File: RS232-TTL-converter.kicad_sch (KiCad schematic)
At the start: 21 parts, among them J1 DE9_Socket, J13 430450600, Q2 BS170F, Q3 BS170F, U4 MAX3232

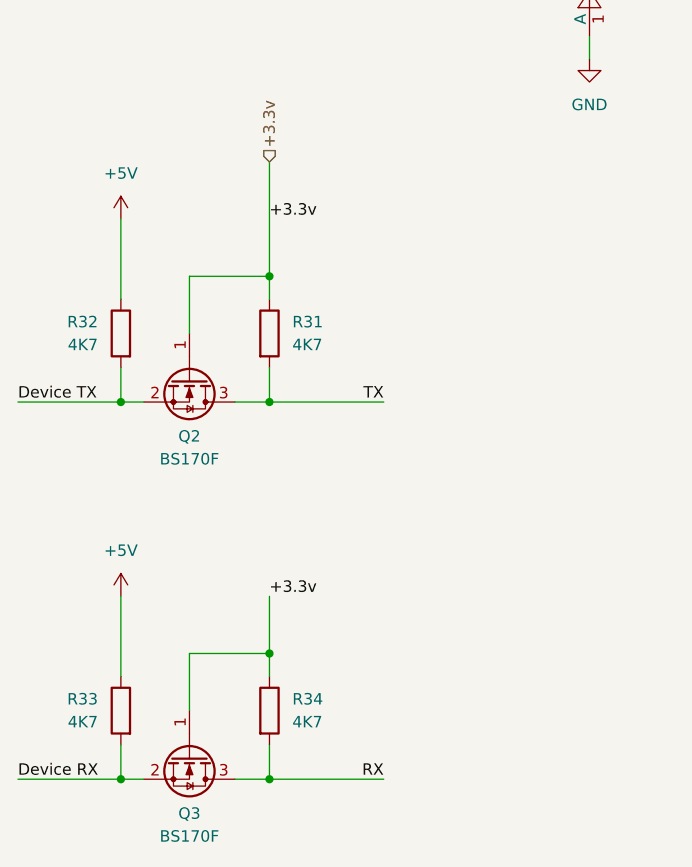
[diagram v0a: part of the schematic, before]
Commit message: Added level shifter
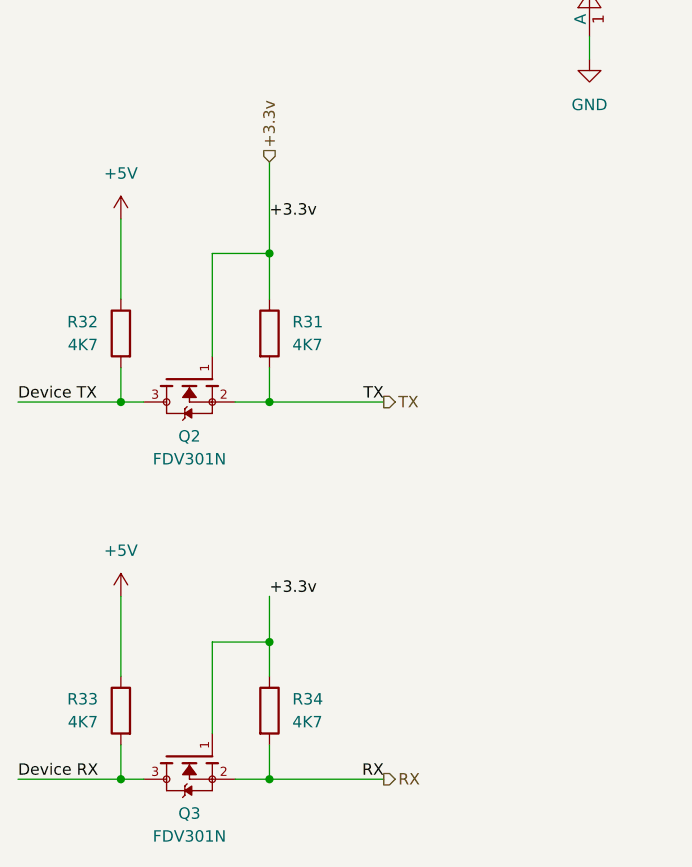
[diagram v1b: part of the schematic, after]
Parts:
- removed Q2, Q3: BS170F, Package_TO_SOT_SMD:SOT-23, symbol Transistor_FET:BS170F
- added Q2, Q3: FDV301N, FDV301N:SOT23, symbol FDV301N:FDV301N
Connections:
- net +3.3v: now also Q2.1, Q3.1
- net Device RX: now also Q3.3
- net Device TX: now also Q2.3
- net RX: now also Q3.2
- net TX: now also Q2.2

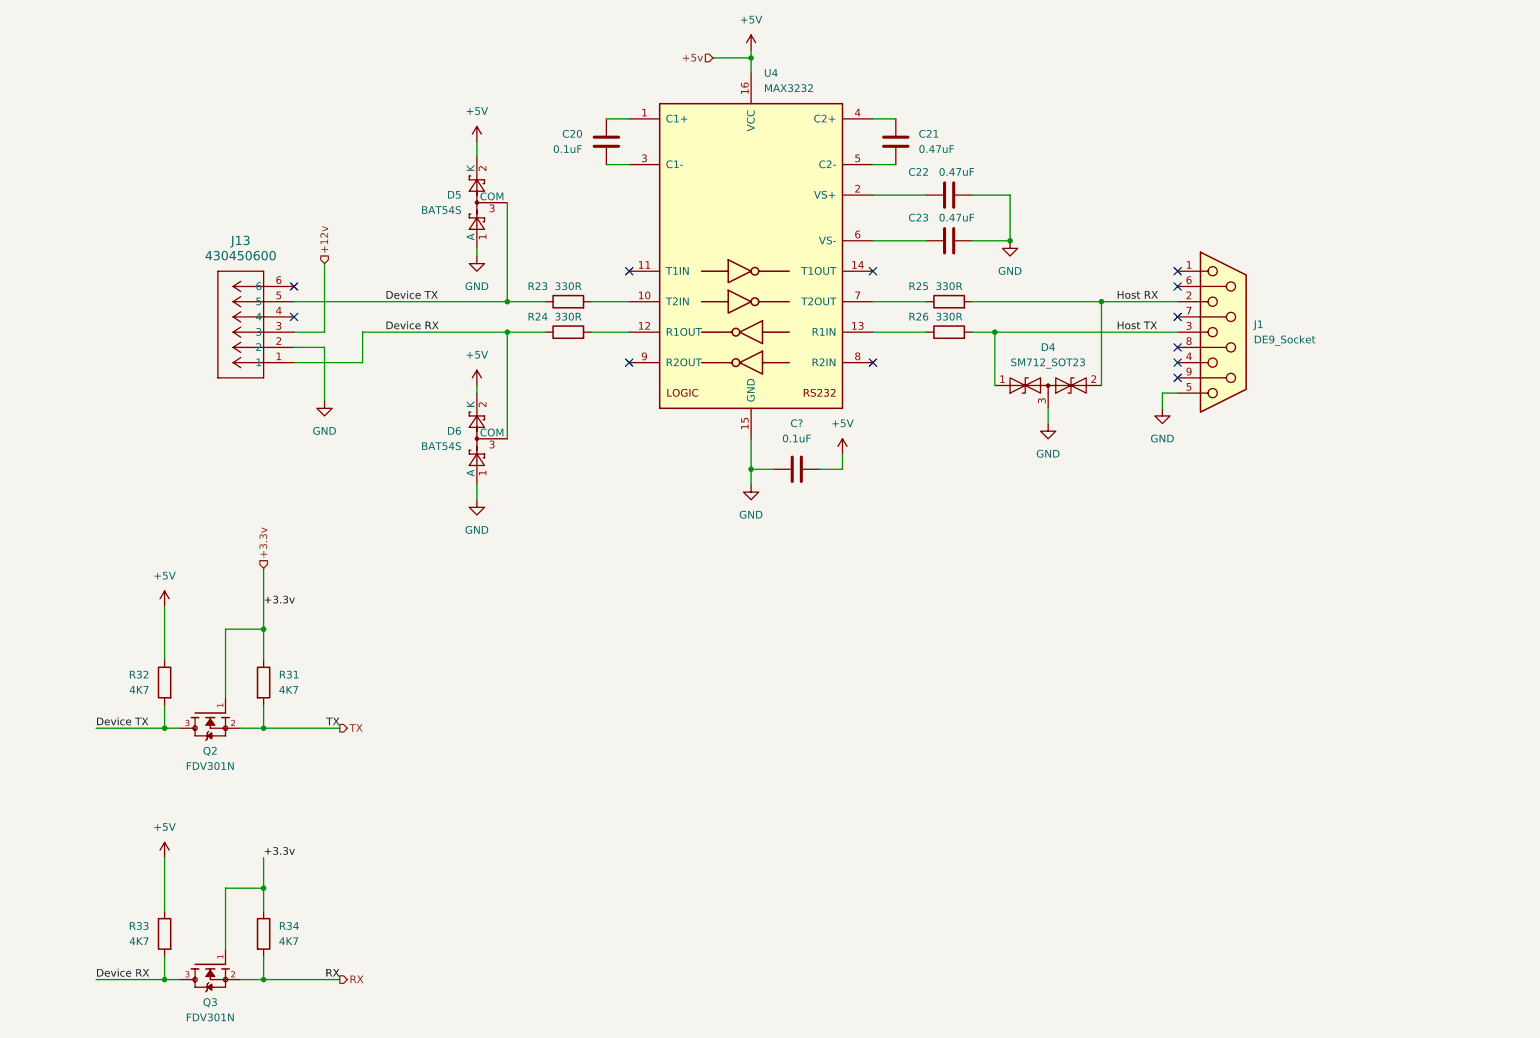
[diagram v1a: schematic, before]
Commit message: added schmitt trigger to level translator
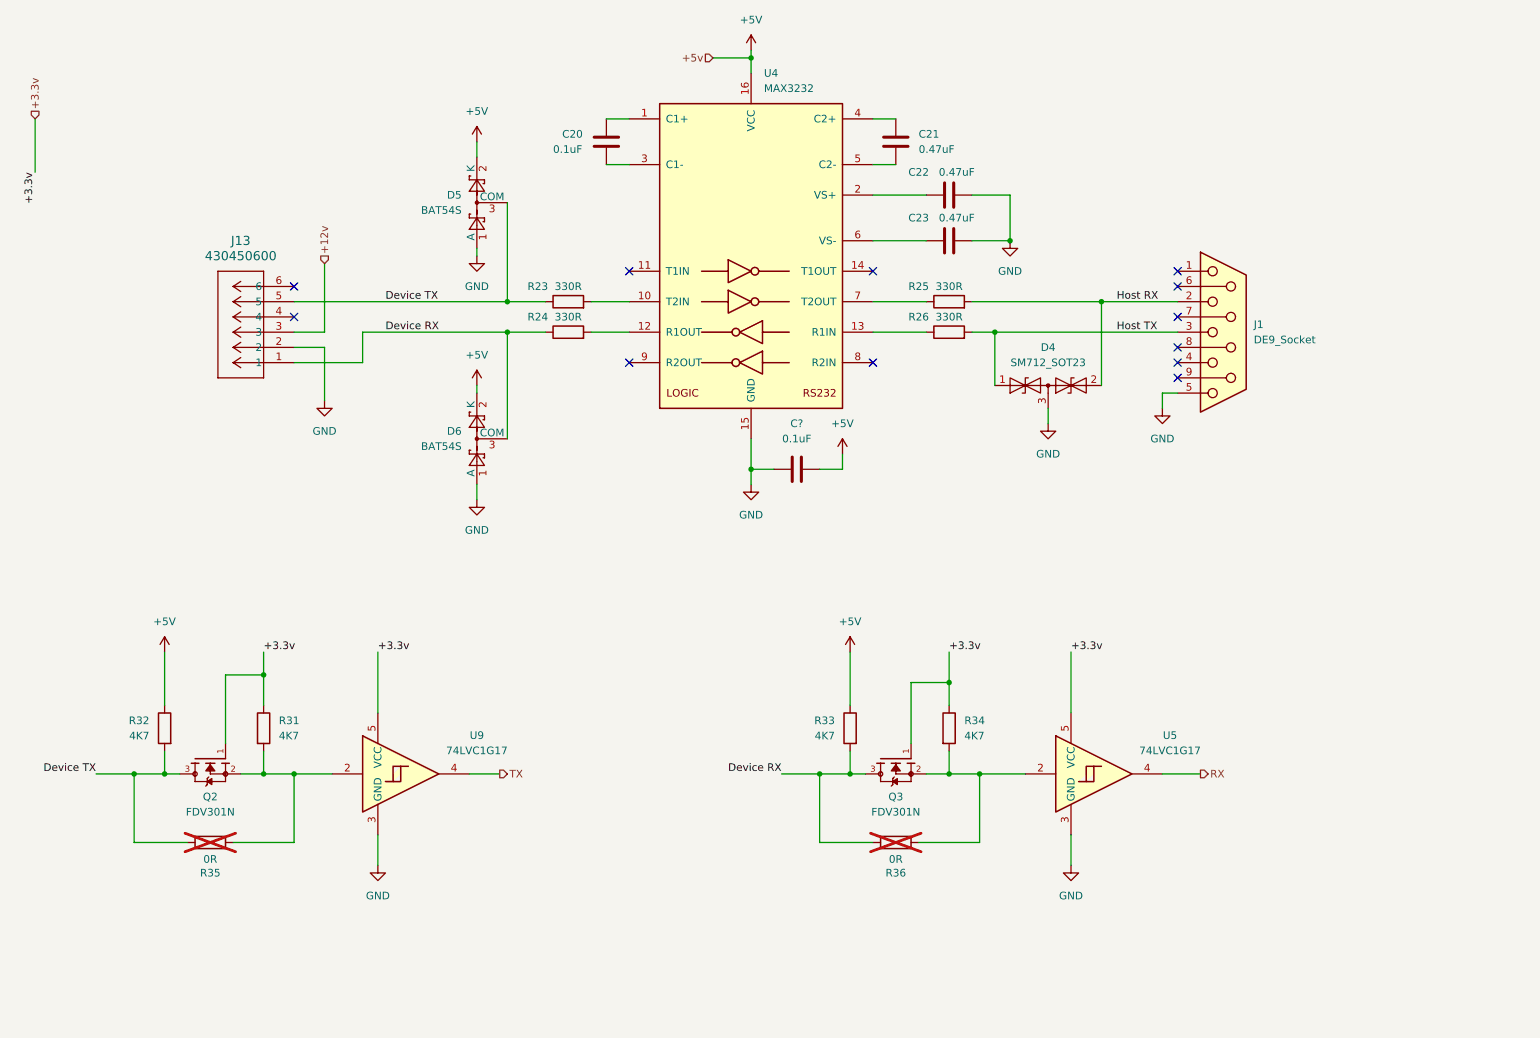
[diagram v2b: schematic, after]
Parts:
- added R35, R36: 0R, Resistor_SMD:R_0603_1608Metric_Pad0.98x0.95mm_HandSolder, symbol Device:R
- added U5, U9: 74LVC1G17, Package_TO_SOT_SMD:SOT-23-5_HandSoldering, symbol 74xGxx:74LVC1G17
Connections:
- net +3.3v: now also U5.5 (VCC), U9.5 (VCC)
- net Device RX: now also R36.2
- net Device TX: now also R35.2
- net GND: now also U5.3 (GND), U9.3 (GND)
- net RX: now also U5.4; no longer Q3.2, R34.2
- net TX: now also U9.4; no longer Q2.2, R31.2
- new net: Q2.2, R31.2, R35.1, U9.2
- new net: Q3.2, R34.2, R36.1, U5.2
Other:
- moved on the sheet: Q2, Q3, R31, R32, R33, R34

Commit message: Need to fix ERC
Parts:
- removed C?: 0.1uF, Capacitor_SMD:C_0603_1608Metric, symbol Device:C
- removed J13: 430450600, molex:molex_43045-0600, symbol molex_43045-0600:430450600
- removed Q2, Q3: FDV301N, FDV301N:SOT23, symbol FDV301N:FDV301N
- removed R31, R32, R33, R34: 4K7, Resistor_SMD:R_0603_1608Metric_Pad0.98x0.95mm_HandSolder, symbol Device:R
- removed R35, R36: 0R, Resistor_SMD:R_0603_1608Metric_Pad0.98x0.95mm_HandSolder, symbol Device:R
- removed U5, U9: 74LVC1G17, Package_TO_SOT_SMD:SOT-23-5_HandSoldering, symbol 74xGxx:74LVC1G17
- added C9: 0.1uF, Capacitor_SMD:C_0603_1608Metric, symbol Device:C
- renumbered C21 to C10, C22 to C11, C23 to C12, C20 to C8, D5 to D3, D6 to D4, D4 to D5, J1 to J6, R23 to R19, R24 to R20, R25 to R21, R26 to R22, U4 to U5
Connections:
- net GND: now also C9.1
- net +5V renamed +5v
- net +5v: now also C9.2
- net Device RX renamed DeviceRX
- net Device TX renamed DeviceTX
- no-connect marks 12 -> 10
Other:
- moved on the sheet: C10, C11, C12, C8, D3, D4, D5, J6, R19, R20, R21, R22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

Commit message: schematic review
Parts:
- added JP4, JP5: SolderJumper_2_Open, Jumper:SolderJumper-2_P1.3mm_Open_RoundedPad1.0x1.5mm, symbol Jumper:SolderJumper_2_Open
- added Q1, Q2: FDV301N, FDV301N:SOT23, symbol FDV301N:FDV301N
- added R10, R7, R8, R9: 4K7, Resistor_SMD:R_0603_1608Metric_Pad0.98x0.95mm_HandSolder, symbol Device:R
- added TP1, TP2: TestPoint, TestPoint:TestPoint_Pad_2.0x2.0mm, symbol Connector:TestPoint
- added U2, U3: 74LVC1G17, Package_TO_SOT_SMD:SOT-23-5_HandSoldering, symbol 74xGxx:74LVC1G17
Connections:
- net +5v: now also R7.1, R8.1
- net DeviceRX: now also JP4.1 (A), Q1.3, R7.2, TP1.1
- net DeviceTX: now also JP5.1 (A), Q2.3, R8.2, TP2.1
- net GND: now also U2.3 (GND), U3.3 (GND)
- new net: JP5.2 (B), Q2.2, R10.2, U2.2
- new net: JP4.2 (B), Q1.2, R9.2, U3.2
- new net +3.3v: Q1.1, Q2.1, R10.1, R9.1, U2.5 (VCC), U3.5 (VCC)
- new net RX: U3.4
- new net TX: U2.4
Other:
- note added: "5v to 3.3v level translator"
- company: (none) -> Astrosystems
- title: (none) -> RS232 to TTL Converter
- moved on the sheet: C10, C11, C12, C8, C9, D3, D4, D5, J6, R19, R20, R21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

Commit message: updated files
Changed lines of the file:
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@@
+	(wire
+		(pts
+			(xy 33.02 25.4) (xy 33.02 34.29)
+		)
+		(stroke
+			(width 0)
+			(type default)
+		)
+	)
 	(wire
 		(pts
@@
 		)
 	)
-	(label "Device RX"
-		(at 119.38 97.79 0)
-		(effects
-			(font
-				(size 1.27 1.27)
-			)
-			(justify left bottom)
-		)
-	)
-	(label "Device TX"
-		(at 119.38 92.71 0)
-		(effects
-			(font
-				(size 1.27 1.27)
-			)
-			(justify left bottom)
-		)
-	)
 	(label "+5v"
 		(at 134.62 106.68 0)
@@
 		)
 	)
-	(label "Device TX"
-		(at 93.98 76.2 180)
-		(effects
-			(font
-				(size 1.27 1.27)
-			)
-			(justify right bottom)
+	(label "+3.3v"
+		(at 33.02 34.29 0)
+		(effects
+			(font
+				(size 1.27 1.27)
+			)
+			(justify left bottom)
 		)
 	)
@@
 			)
 			(justify left bottom)
-		)
-	)
-	(label "Device RX"
-		(at 93.98 127 180)
-		(effects
-			(font
-				(size 1.27 1.27)
-			)
-			(justify right bottom)
 		)
 	)
@@
 	(hierarchical_label "DeviceTX"
 		(shape input)
+		(at 119.38 92.71 180)
+		(effects
+			(font
+				(size 1.27 1.27)
+			)
+			(justify right)
+		)
+	)
+	(hierarchical_label "DeviceTX"
+		(shape input)
 		(at 95.25 76.2 0)
 		(effects
@@
 		)
 	)
+	(hierarchical_label "+3.3v"
+		(shape input)
+		(at 33.02 25.4 90)
+		(effects
+			(font
+				(size 1.27 1.27)
+			)
+			(justify left)
+		)
+	)
+	(hierarchical_label "DeviceRX"
+		(shape input)
+		(at 119.38 97.79 180)
+		(effects
+			(font
+				(size 1.27 1.27)
+			)
+			(justify right)
+		)
+	)
